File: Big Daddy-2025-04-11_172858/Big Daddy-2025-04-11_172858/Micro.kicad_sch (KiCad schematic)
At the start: 25 parts, among them Q1 2N7002, U1 MAX33054EASA+T, U2 ESP32-S3-DevKitC, U3 ESP32-S3-DevKitC

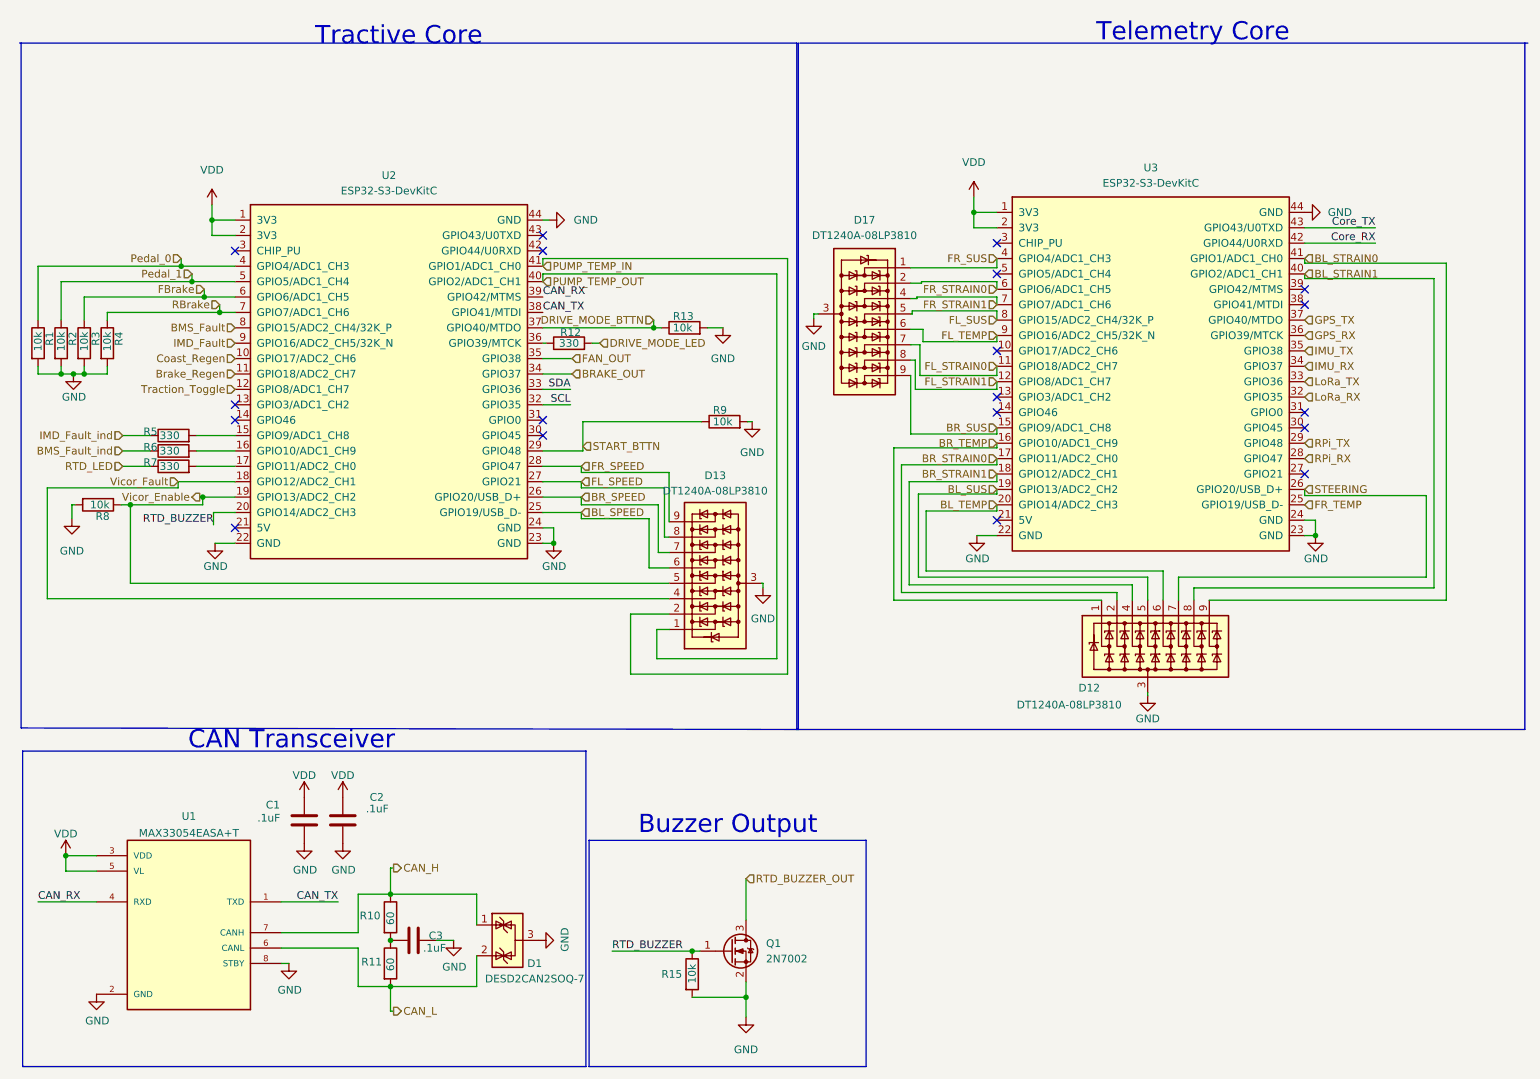
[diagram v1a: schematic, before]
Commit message: diode arrays deleted
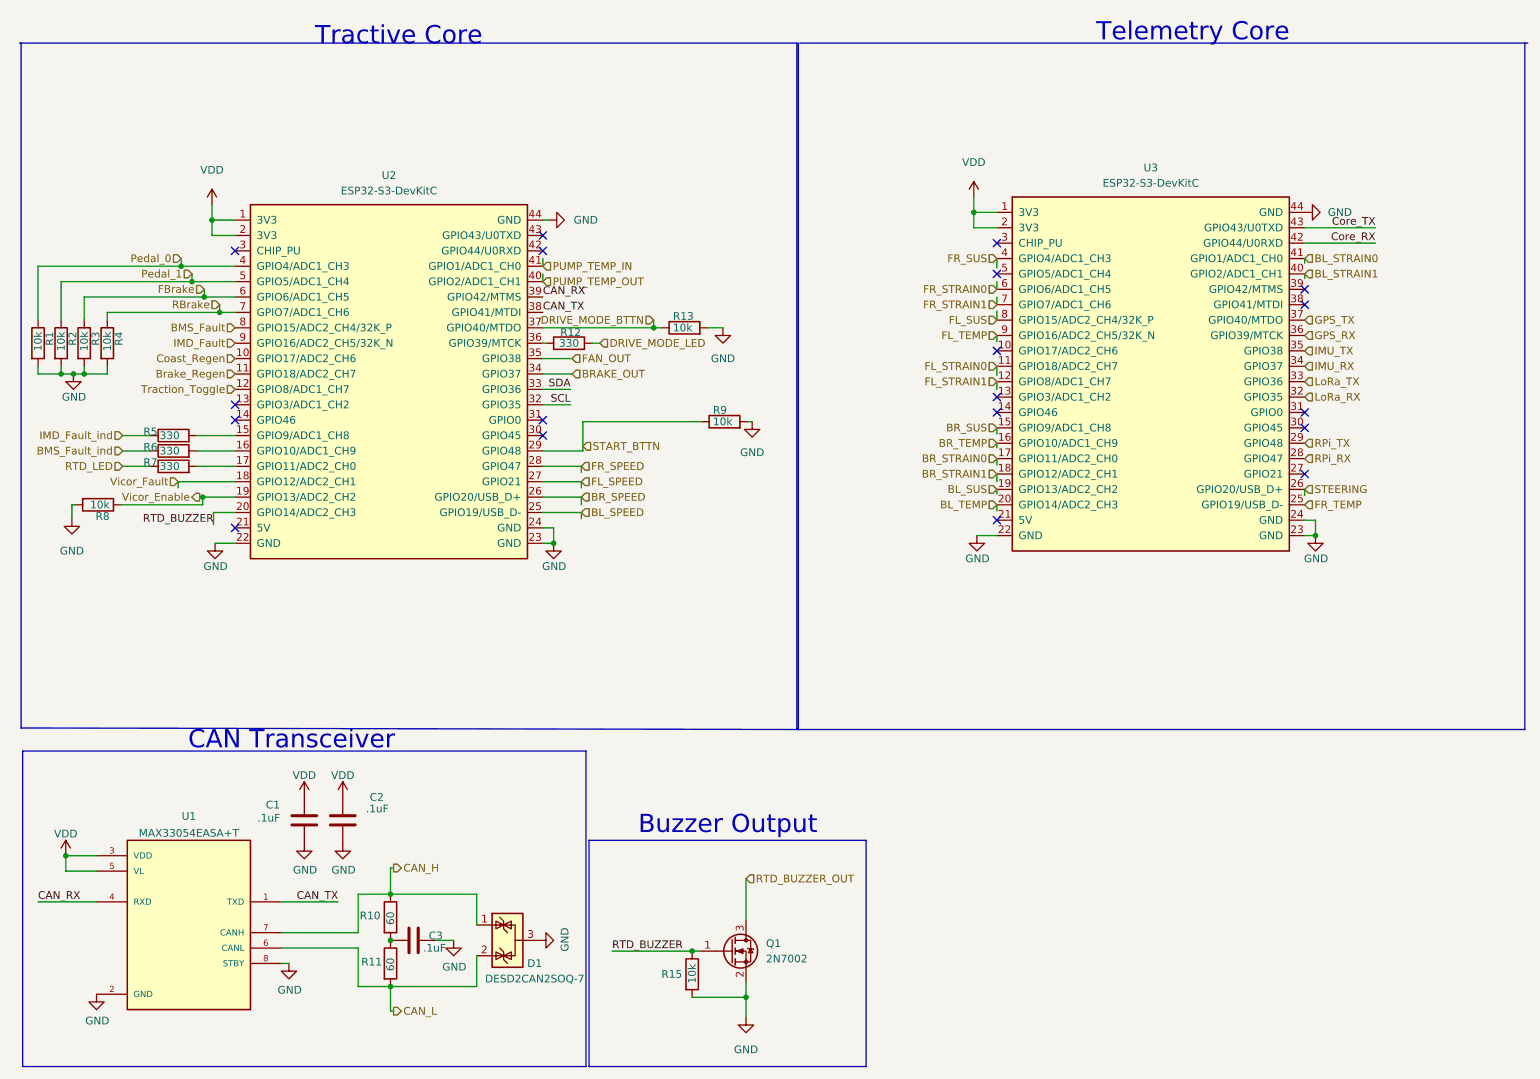
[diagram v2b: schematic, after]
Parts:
- removed D12, D13, D17: DT1240A-08LP3810, Package_DFN_QFN:UDFN-9_1.0x3.8mm_P0.5mm, symbol Power_Protection:DT1240A-08LP3810

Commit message: BMS Indicator
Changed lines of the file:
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@@
-	(wire
-		(pts
-			(xy 40.894 103.886) (xy 40.894 102.87)
-		)
-		(stroke
-			(width 0)
-			(type default)
-		)
-	)
 	(wire
 		(pts

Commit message: all the bs
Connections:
- net PUMP_TEMP_OUT is gone; now on net PUMP_TEMP_IN: U2.40 (GPIO2/ADC1_CH1)
- net TSSI_Fault: now reaches U2.13 (GPIO3/ADC1_CH2)
- no-connect marks 19 -> 18
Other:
- moved on the sheet: U2
